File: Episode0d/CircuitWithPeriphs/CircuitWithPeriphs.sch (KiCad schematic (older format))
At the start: 0 parts

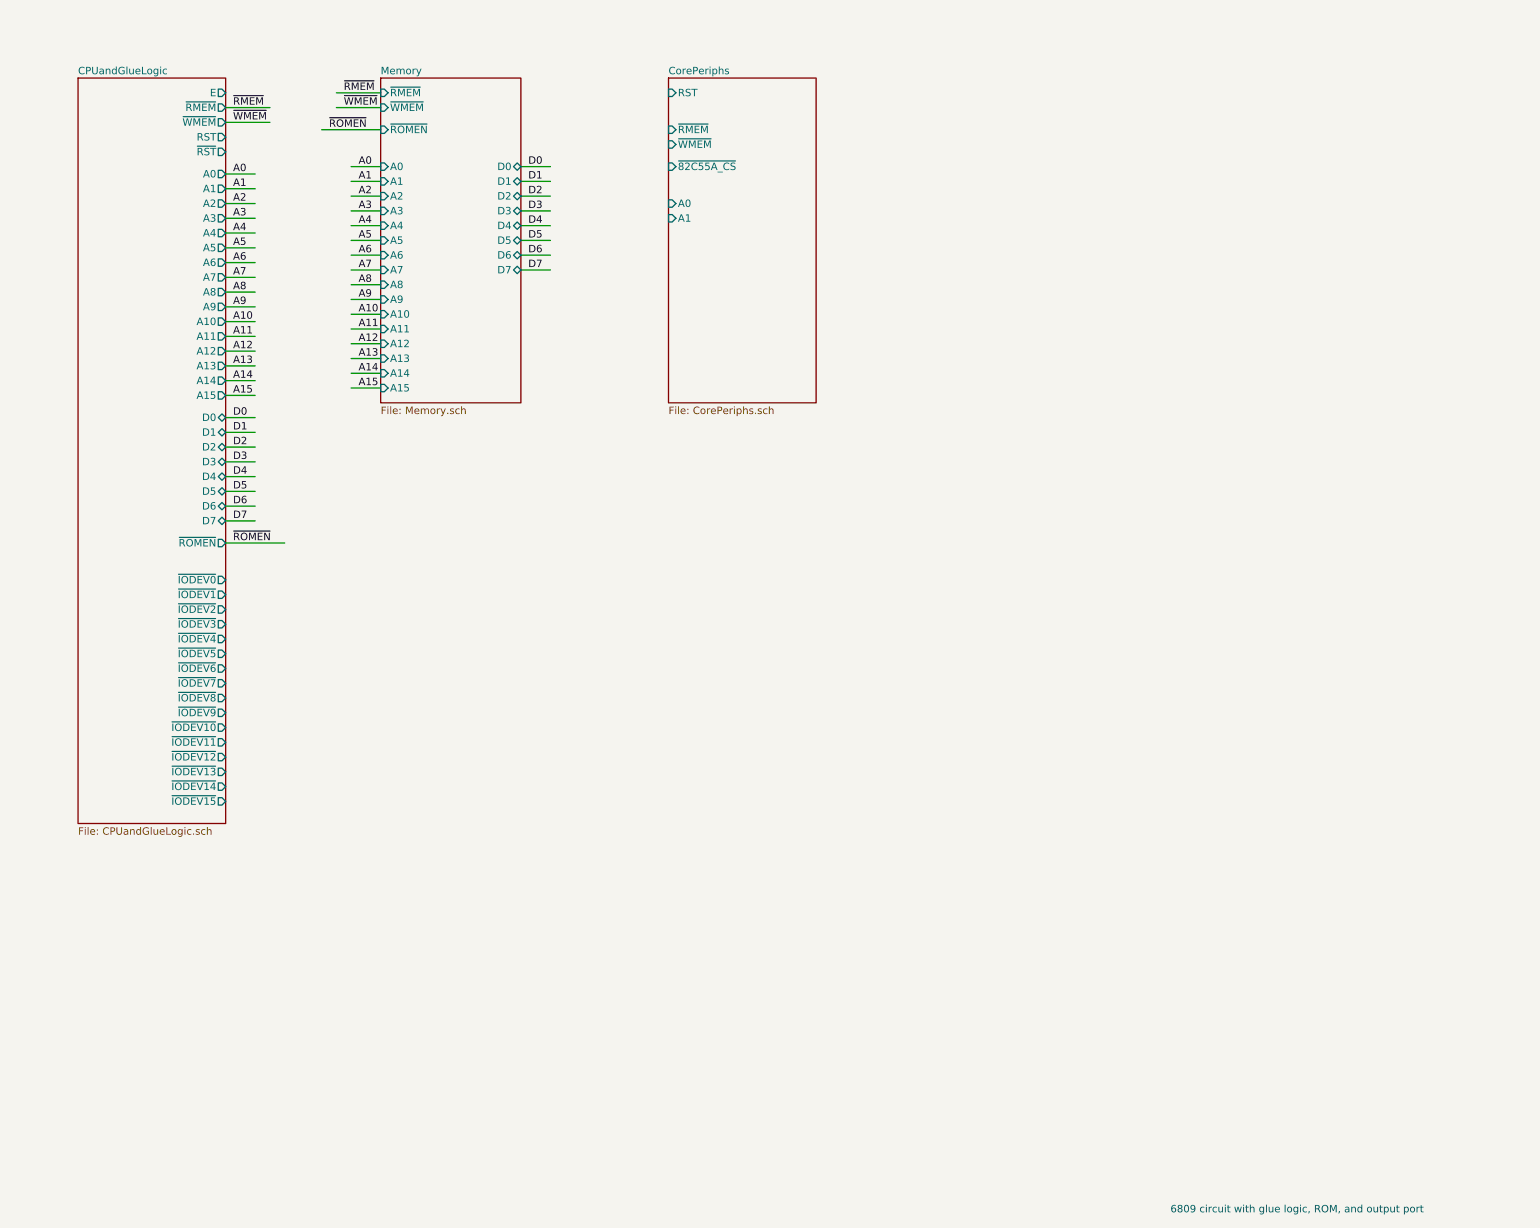
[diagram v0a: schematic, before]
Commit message: added i82c54, various schematic cleanups
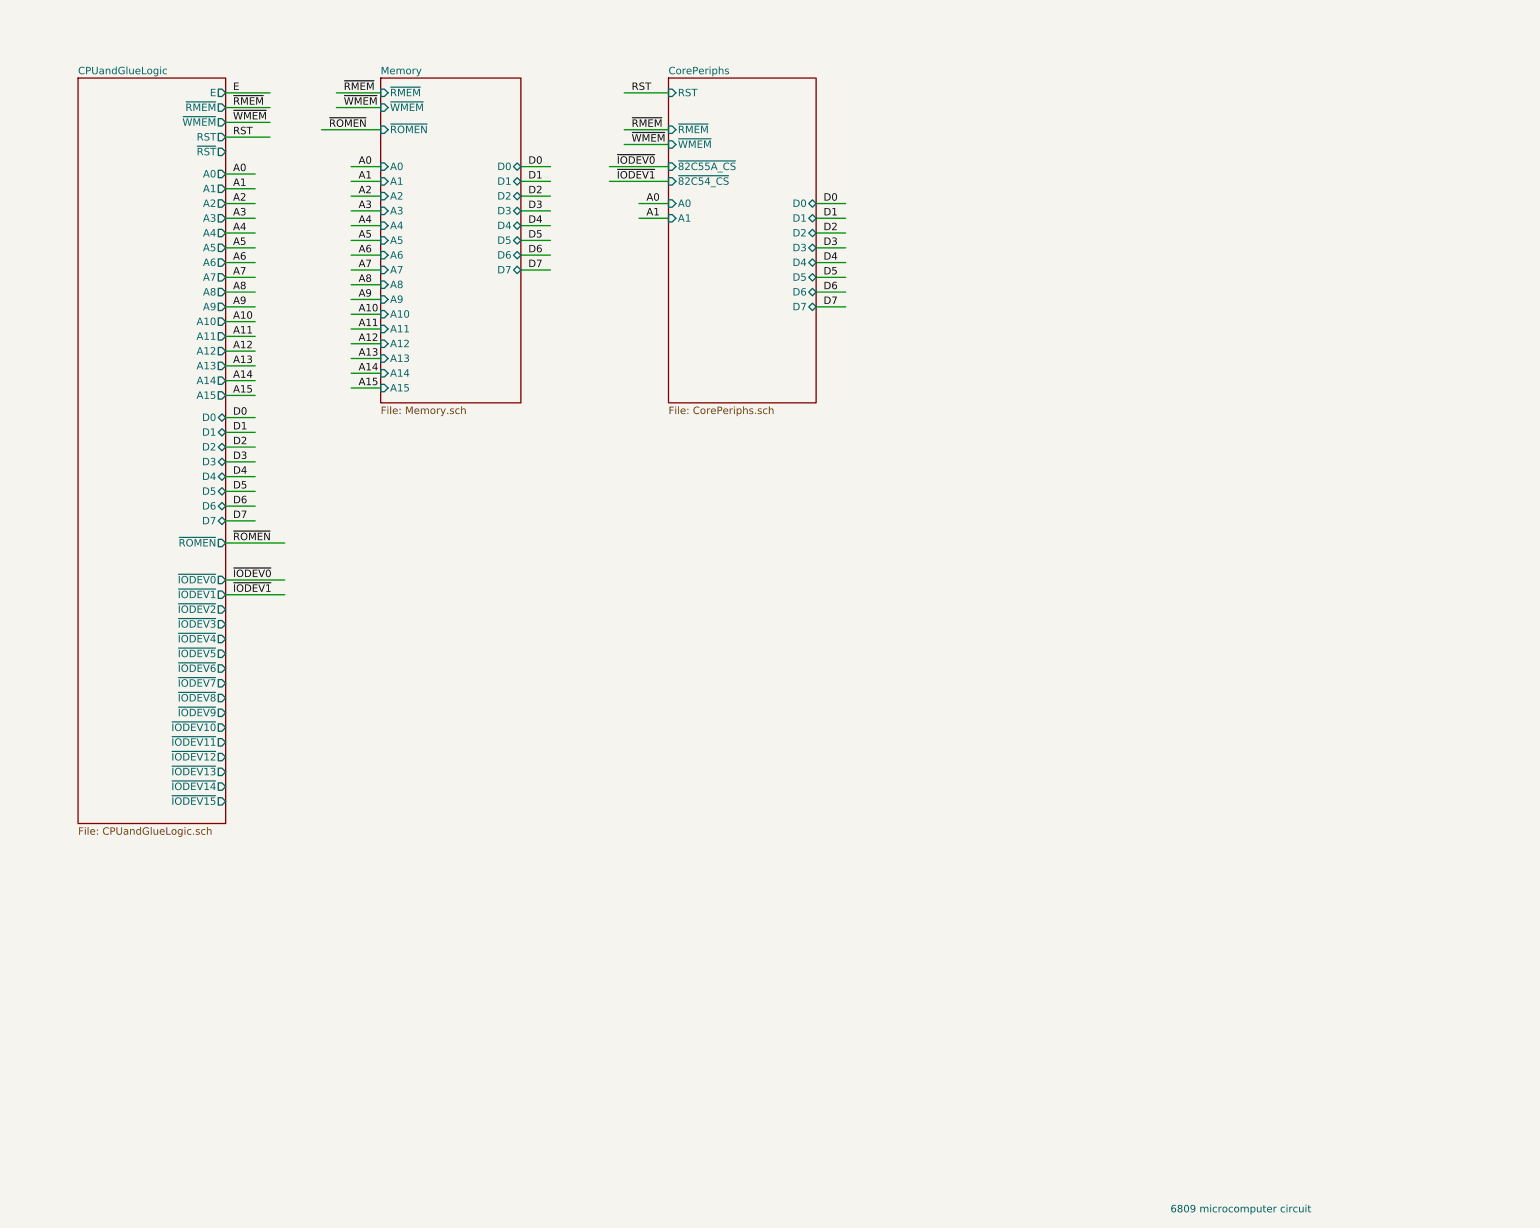
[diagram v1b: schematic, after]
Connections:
- net labels added: E, RST, ~IODEV0, ~IODEV1
- wire segments 54 -> 73
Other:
- note added: "6809 microcomputer circuit"
- note removed: "6809 circuit with glue logic, ROM, and output port"
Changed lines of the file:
@@
 $EndDescr
 Text Notes 9600 9400 0    50   ~ 0
-6809 circuit with glue logic, ROM, and output port
+6809 microcomputer circuit
 $Sheet
 S 2200 1700 1000 5050
@@
 F6 "A0" I L 6200 2550 50
 F7 "A1" I L 6200 2650 50
+F8 "D0" B R 7200 2550 50
+F9 "D1" B R 7200 2650 50
+F10 "D2" B R 7200 2750 50
+F11 "D3" B R 7200 2850 50
+F12 "D4" B R 7200 2950 50
+F13 "D5" B R 7200 3050 50
+F14 "D6" B R 7200 3150 50
+F15 "D7" B R 7200 3250 50
+F16 "~82C54_CS" I L 6200 2400 50
 $EndSheet
+Wire Wire Line
+	3200 5100 3600 5100
+Wire Wire Line
+	3200 5200 3600 5200
+Text Label 3250 5100 0    50   ~ 0
+~IODEV0
+Text Label 3250 5200 0    50   ~ 0
+~IODEV1
+Wire Wire Line
+	5800 2300 6200 2300
+Wire Wire Line
+	5800 2400 6200 2400
+Text Label 5850 2300 0    50   ~ 0
+~IODEV0
+Text Label 5850 2400 0    50   ~ 0
+~IODEV1
+Wire Wire Line
+	6000 2550 6200 2550
+Wire Wire Line
+	6000 2650 6200 2650
+Text Label 6050 2550 0    50   ~ 0
+A0
+Text Label 6050 2650 0    50   ~ 0
+A1
+Wire Wire Line
+	7200 2550 7400 2550
+Wire Wire Line
+	7200 2650 7400 2650
+Wire Wire Line
+	7200 2750 7400 2750
+Wire Wire Line
+	7200 2850 7400 2850
+Wire Wire Line
+	7200 2950 7400 2950
+Wire Wire Line
+	7200 3050 7400 3050
+Wire Wire Line
+	7200 3150 7400 3150
+Wire Wire Line
+	7200 3250 7400 3250
+Text Label 7250 2550 0    50   ~ 0
+D0
+Text Label 7250 2650 0    50   ~ 0
+D1
+Text Label 7250 2750 0    50   ~ 0
+D2
+Text Label 7250 2850 0    50   ~ 0
+D3
+Text Label 7250 2950 0    50   ~ 0
+D4
+Text Label 7250 3050 0    50   ~ 0
+D5
+Text Label 7250 3150 0    50   ~ 0
+D6
+Text Label 7250 3250 0    50   ~ 0
+D7
+Wire Wire Line
+	5900 2050 6200 2050
+Wire Wire Line
+	5900 2150 6200 2150
+Text Label 5950 2050 0    50   ~ 0
+~RMEM~
+Text Label 5950 2150 0    50   ~ 0
+~WMEM~
+Wire Wire Line
+	3200 2100 3500 2100
+Text Label 3250 2100 0    50   ~ 0
+RST
+Wire Wire Line
+	6200 1800 5900 1800
+Text Label 5950 1800 0    50   ~ 0
+RST
+Wire Wire Line
+	3200 1800 3500 1800
+Text Label 3250 1800 0    50   ~ 0
+E
 $EndSCHEMATC

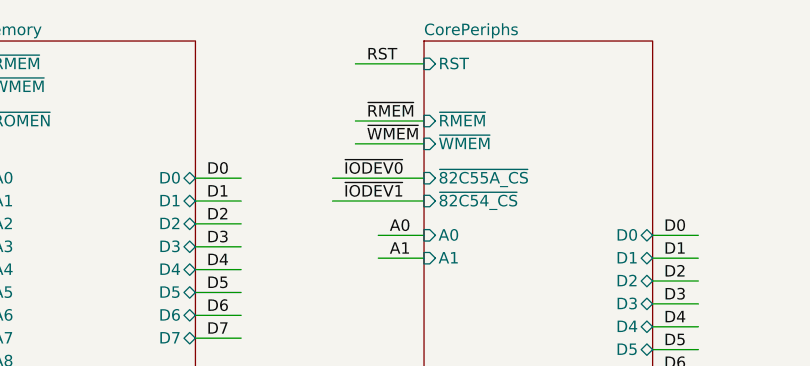
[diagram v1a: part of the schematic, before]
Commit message: use E signal as timer input for 82c54
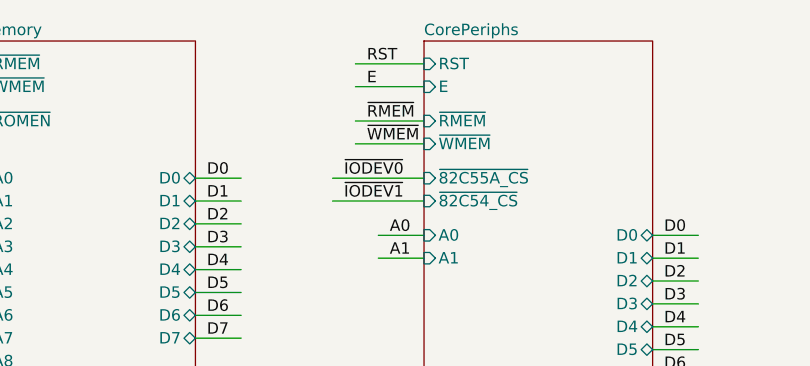
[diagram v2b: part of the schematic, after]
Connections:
- wire segments 73 -> 74
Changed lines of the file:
@@
 F15 "D7" B R 7200 3250 50
 F16 "~82C54_CS" I L 6200 2400 50
+F17 "E" I L 6200 1900 50
 $EndSheet
 Wire Wire Line
@@
 Text Label 3250 1800 0    50   ~ 0
 E
+Wire Wire Line
+	6200 1900 5900 1900
+Text Label 5950 1900 0    50   ~ 0
+E
 $EndSCHEMATC

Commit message: working on integrating ACIA device
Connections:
- net labels added: R~W, ~IODEV2
- wire segments 74 -> 78
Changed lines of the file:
@@
 F0 "CPUandGlueLogic" 50
 F1 "CPUandGlueLogic.sch" 50
-F2 "A0" O R 3200 2350 50
-F3 "A1" O R 3200 2450 50
-F4 "A2" O R 3200 2550 50
-F5 "A3" O R 3200 2650 50
-F6 "A4" O R 3200 2750 50
-F7 "A5" O R 3200 2850 50
-F8 "A6" O R 3200 2950 50
-F9 "A7" O R 3200 3050 50
-F10 "A8" O R 3200 3150 50
-F11 "A9" O R 3200 3250 50
-F12 "A10" O R 3200 3350 50
-F13 "A11" O R 3200 3450 50
-F14 "A12" O R 3200 3550 50
-F15 "A13" O R 3200 3650 50
-F16 "A14" O R 3200 3750 50
-F17 "A15" O R 3200 3850 50
-F18 "D0" B R 3200 4000 50
-F19 "D1" B R 3200 4100 50
-F20 "D2" B R 3200 4200 50
-F21 "D3" B R 3200 4300 50
-F22 "D4" B R 3200 4400 50
-F23 "D5" B R 3200 4500 50
-F24 "D6" B R 3200 4600 50
-F25 "D7" B R 3200 4700 50
+F2 "A0" O R 3200 2450 50
+F3 "A1" O R 3200 2550 50
+F4 "A2" O R 3200 2650 50
+F5 "A3" O R 3200 2750 50
+F6 "A4" O R 3200 2850 50
+F7 "A5" O R 3200 2950 50
+F8 "A6" O R 3200 3050 50
+F9 "A7" O R 3200 3150 50
+F10 "A8" O R 3200 3250 50
+F11 "A9" O R 3200 3350 50
+F12 "A10" O R 3200 3450 50
+F13 "A11" O R 3200 3550 50
+F14 "A12" O R 3200 3650 50
+F15 "A13" O R 3200 3750 50
+F16 "A14" O R 3200 3850 50
+F17 "A15" O R 3200 3950 50
+F18 "D0" B R 3200 4100 50
+F19 "D1" B R 3200 4200 50
+F20 "D2" B R 3200 4300 50
+F21 "D3" B R 3200 4400 50
+F22 "D4" B R 3200 4500 50
+F23 "D5" B R 3200 4600 50
+F24 "D6" B R 3200 4700 50
+F25 "D7" B R 3200 4800 50
 F26 "E" O R 3200 1800 50
 F27 "~RMEM~" O R 3200 1900 50
@@
 F45 "~IODEV14~" O R 3200 6500 50
 F46 "~IODEV15~" O R 3200 6600 50
-F47 "~ROMEN~" O R 3200 4850 50
+F47 "~ROMEN~" O R 3200 4950 50
+F48 "R~W" O R 3200 2300 50
 $EndSheet
 $Sheet
@@
 $EndSheet
 Wire Wire Line
-	3200 2350 3400 2350
-Wire Wire Line
 	3200 2450 3400 2450
 Wire Wire Line
@@
 Wire Wire Line
 	3200 3850 3400 3850
-Text Label 3250 2350 0    50   ~ 0
+Wire Wire Line
+	3200 3950 3400 3950
+Text Label 3250 2450 0    50   ~ 0
 A0
-Text Label 3250 2450 0    50   ~ 0
+Text Label 3250 2550 0    50   ~ 0
 A1
-Text Label 3250 2550 0    50   ~ 0
+Text Label 3250 2650 0    50   ~ 0
 A2
-Text Label 3250 2650 0    50   ~ 0
+Text Label 3250 2750 0    50   ~ 0
 A3
-Text Label 3250 2750 0    50   ~ 0
+Text Label 3250 2850 0    50   ~ 0
 A4
-Text Label 3250 2850 0    50   ~ 0
+Text Label 3250 2950 0    50   ~ 0
 A5
-Text Label 3250 2950 0    50   ~ 0
+Text Label 3250 3050 0    50   ~ 0
 A6
-Text Label 3250 3050 0    50   ~ 0
+Text Label 3250 3150 0    50   ~ 0
 A7
-Text Label 3250 3150 0    50   ~ 0
+Text Label 3250 3250 0    50   ~ 0
 A8
-Text Label 3250 3250 0    50   ~ 0
+Text Label 3250 3350 0    50   ~ 0
 A9
-Text Label 3250 3350 0    50   ~ 0
+Text Label 3250 3450 0    50   ~ 0
 A10
-Text Label 3250 3450 0    50   ~ 0
+Text Label 3250 3550 0    50   ~ 0
 A11
-Text Label 3250 3550 0    50   ~ 0
+Text Label 3250 3650 0    50   ~ 0
 A12
-Text Label 3250 3650 0    50   ~ 0
+Text Label 3250 3750 0    50   ~ 0
 A13
-Text Label 3250 3750 0    50   ~ 0
+Text Label 3250 3850 0    50   ~ 0
 A14
-Text Label 3250 3850 0    50   ~ 0
+Text Label 3250 3950 0    50   ~ 0
 A15
 Wire Wire Line
@@
 A14
 Wire Wire Line
-	3200 4000 3400 4000
-Wire Wire Line
 	3200 4100 3400 4100
 Wire Wire Line
@@
 Wire Wire Line
 	3200 4700 3400 4700
-Text Label 3250 4000 0    50   ~ 0
+Wire Wire Line
+	3200 4800 3400 4800
+Text Label 3250 4100 0    50   ~ 0
 D0
-Text Label 3250 4100 0    50   ~ 0
+Text Label 3250 4200 0    50   ~ 0
 D1
-Text Label 3250 4200 0    50   ~ 0
+Text Label 3250 4300 0    50   ~ 0
 D2
-Text Label 3250 4300 0    50   ~ 0
+Text Label 3250 4400 0    50   ~ 0
 D3
-Text Label 3250 4400 0    50   ~ 0
+Text Label 3250 4500 0    50   ~ 0
 D4
-Text Label 3250 4500 0    50   ~ 0
+Text Label 3250 4600 0    50   ~ 0
 D5
-Text Label 3250 4600 0    50   ~ 0
+Text Label 3250 4700 0    50   ~ 0
 D6
-Text Label 3250 4700 0    50   ~ 0
+Text Label 3250 4800 0    50   ~ 0
 D7
 Wire Wire Line
@@
 ~WMEM~
 Wire Wire Line
-	3200 4850 3600 4850
-Text Label 3250 4850 0    50   ~ 0
+	3200 4950 3600 4950
+Text Label 3250 4950 0    50   ~ 0
 ~ROMEN~
 Wire Wire Line
@@
 F1 "CorePeriphs.sch" 50
 F2 "RST" I L 6200 1800 50
-F3 "~82C55A_CS" I L 6200 2300 50
-F4 "~RMEM" I L 6200 2050 50
-F5 "~WMEM" I L 6200 2150 50
-F6 "A0" I L 6200 2550 50
-F7 "A1" I L 6200 2650 50
+F3 "~82C55A_CS" I L 6200 2400 50
+F4 "~RMEM" I L 6200 2150 50
+F5 "~WMEM" I L 6200 2250 50
+F6 "A0" I L 6200 2750 50
+F7 "A1" I L 6200 2850 50
 F8 "D0" B R 7200 2550 50
 F9 "D1" B R 7200 2650 50
@@
 F14 "D6" B R 7200 3150 50
 F15 "D7" B R 7200 3250 50
-F16 "~82C54_CS" I L 6200 2400 50
+F16 "~82C54_CS" I L 6200 2500 50
 F17 "E" I L 6200 1900 50
+F18 "R~W" I L 6200 2000 50
+F19 "~6850_CS" I L 6200 2600 50
 $EndSheet
 Wire Wire Line
@@
 ~IODEV1
 Wire Wire Line
-	5800 2300 6200 2300
-Wire Wire Line
 	5800 2400 6200 2400
-Text Label 5850 2300 0    50   ~ 0
+Wire Wire Line
+	5800 2500 6200 2500
+Text Label 5850 2400 0    50   ~ 0
 ~IODEV0
-Text Label 5850 2400 0    50   ~ 0
+Text Label 5850 2500 0    50   ~ 0
 ~IODEV1
 Wire Wire Line
-	6000 2550 6200 2550
-Wire Wire Line
-	6000 2650 6200 2650
-Text Label 6050 2550 0    50   ~ 0
+	6000 2750 6200 2750
+Wire Wire Line
+	6000 2850 6200 2850
+Text Label 6050 2750 0    50   ~ 0
 A0
-Text Label 6050 2650 0    50   ~ 0
+Text Label 6050 2850 0    50   ~ 0
 A1
 Wire Wire Line
@@
 D7
 Wire Wire Line
-	5900 2050 6200 2050
-Wire Wire Line
 	5900 2150 6200 2150
-Text Label 5950 2050 0    50   ~ 0
+Wire Wire Line
+	5900 2250 6200 2250
+Text Label 5950 2150 0    50   ~ 0
 ~RMEM~
-Text Label 5950 2150 0    50   ~ 0
+Text Label 5950 2250 0    50   ~ 0
 ~WMEM~
 Wire Wire Line
@@
 Text Label 5950 1900 0    50   ~ 0
 E
+Wire Wire Line
+	3200 2300 3500 2300
+Text Label 3250 2300 0    50   ~ 0
+R~W
+Wire Wire Line
+	6200 2000 5900 2000
+Text Label 5950 2000 0    50   ~ 0
+R~W
+Wire Wire Line
+	3200 5300 3600 5300
+Text Label 3250 5300 0    50   ~ 0
+~IODEV2
+Wire Wire Line
+	5800 2600 6200 2600
+Text Label 5850 2600 0    50   ~ 0
+~IODEV2
 $EndSCHEMATC
